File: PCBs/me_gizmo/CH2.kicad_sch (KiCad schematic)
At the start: 10 parts, among them J2 PushButton_Terminal_01x06, U1 ADG714, U2 ADG714, U3 ADG714

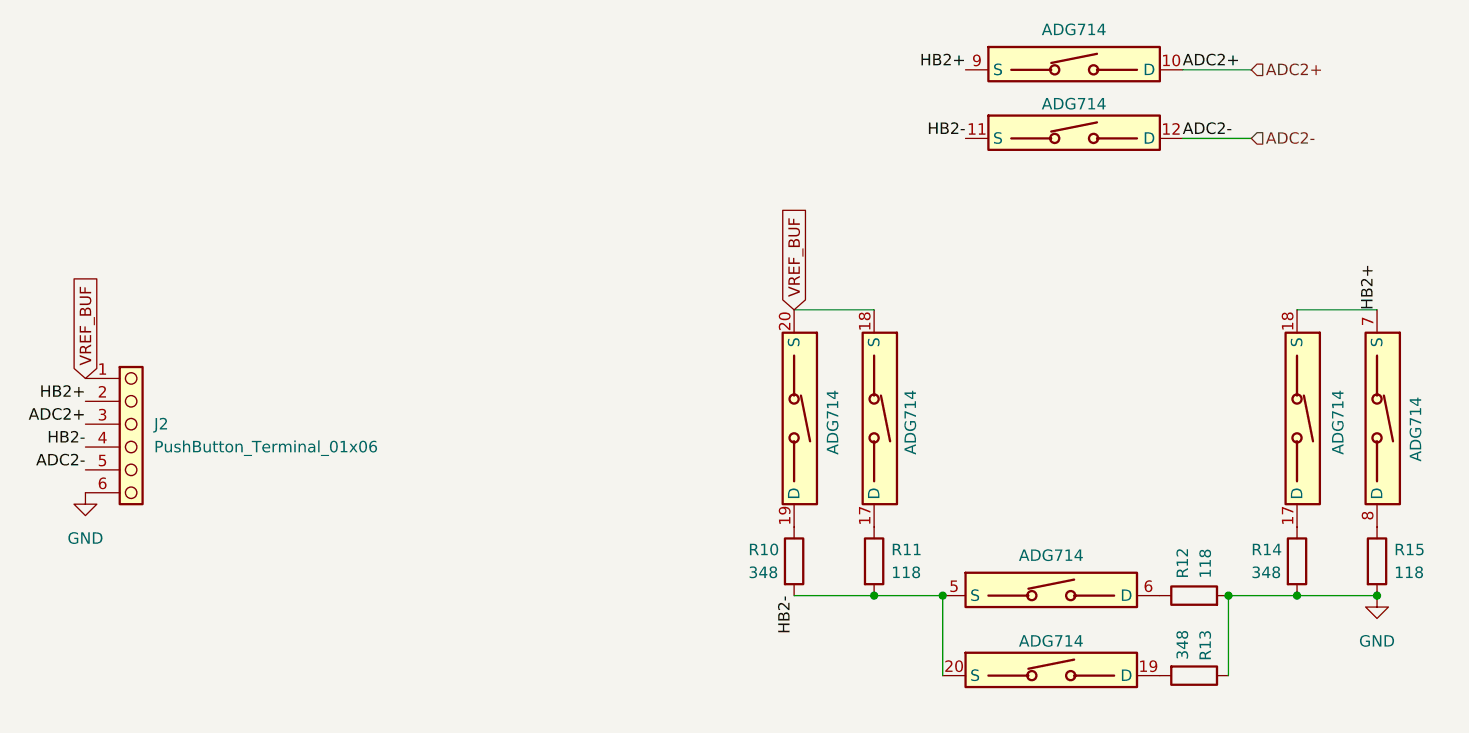
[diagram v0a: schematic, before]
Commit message: Completed first draft of integrated measurement unit
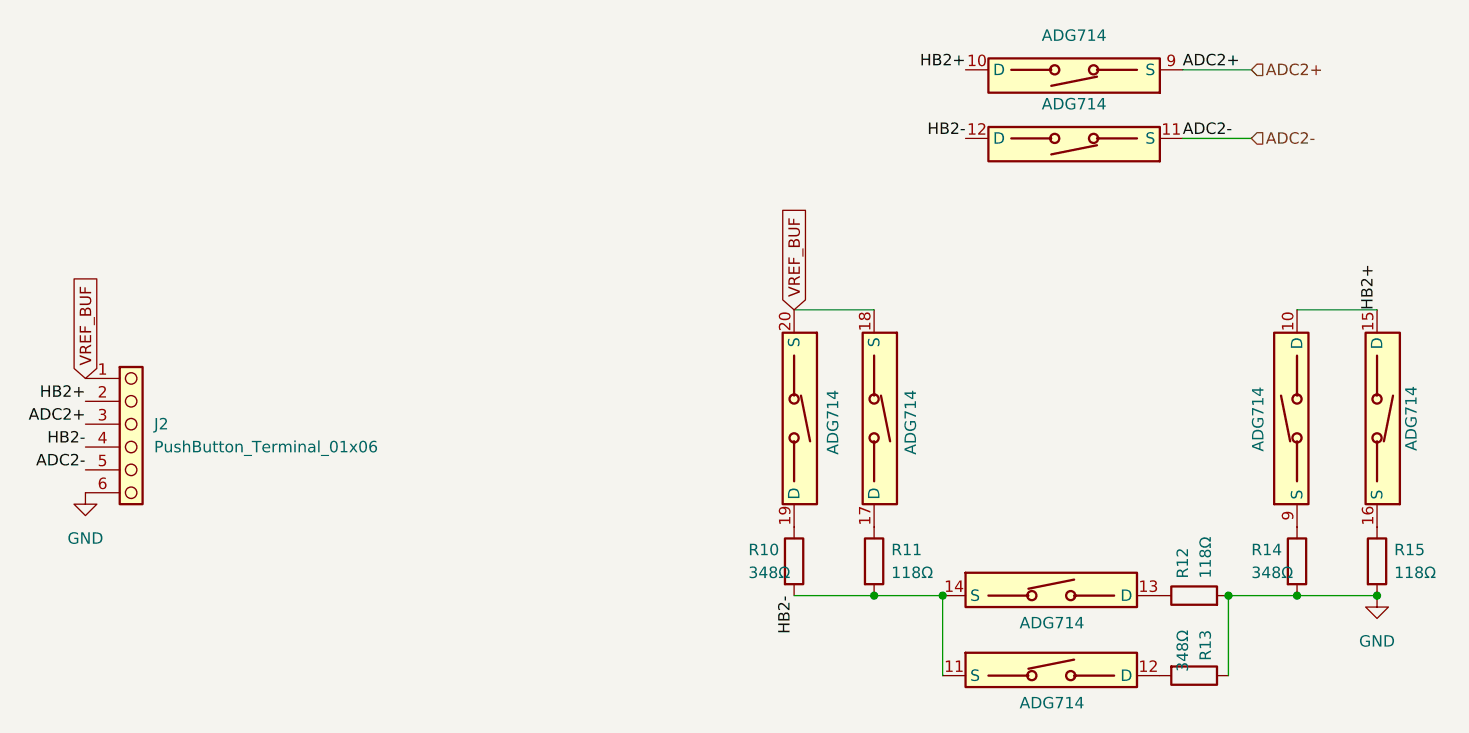
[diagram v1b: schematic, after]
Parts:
- removed U2: ADG714, Package_SO:TSSOP-24_4.4x7.8mm_P0.65mm, symbol Analog_Switch:ADG714
- added U2: ADG714, Package_SO:TSSOP-24_4.4x7.8mm_P0.65mm, symbol Analog_Switch:ADG714
- J2: footprint WAGO:CONN5_233-505_WAG -> TerminalBlock_WAGO:TerminalBlock_WAGO_233-506_2x06_P2.54mm
- R10, R13, R14: value 348 -> 348Ω
- R11, R12, R15: value 118 -> 118Ω
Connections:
- net ADC2+: now also U3.9 (S); no longer U3.10 (D)
- net ADC2-: now also U3.11 (S); no longer U3.12 (D)
- net HB2+: now also U3.10 (D), U2.10 (D), U2.15 (D); no longer U3.9 (S)
- net HB2-: now also U3.12 (D), U2.11 (S), U2.14 (S); no longer U3.11 (S)
- net at R13.2: now also U2.12 (D)
- net at R12.1: now also U2.13 (D)
- net at R14.1: now also U2.9 (S)
- net at R15.1: now also U2.16 (S)
